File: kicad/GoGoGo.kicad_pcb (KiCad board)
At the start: 2 copper layers, 20.1 x 21.3 mm, 8 parts, among them P1 Vcc, P2 Input, P3 Output, U1 TB6593FNG

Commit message: Main layout done
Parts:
- moved C1 1.02 mm to (160.8, 86.9)
- moved C2 0.76 mm to (165.4, 86.6)
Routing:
- net /IN2: track 18.8 -> 14.0 mm
- net Net-(C1-Pad1): track 19.4 -> 17.3 mm
- net /IN1: track 13.8 -> 13.2 mm
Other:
- board text added: "GND"
- board text added: "IN1"
- board text added: "IN2"
- board text added: "Moto Driver Rev 2L.1"
- board text added: "O1"
- board text added: "O2"
- board text added: "PMW"
- board text added: "STBY"
- board text added: "Vcc"

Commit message: Gerbers created
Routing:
- net GND: track 0.00 -> 117.2 mm, vias 0 -> 84
- added copper zone on B.Cu, net GND

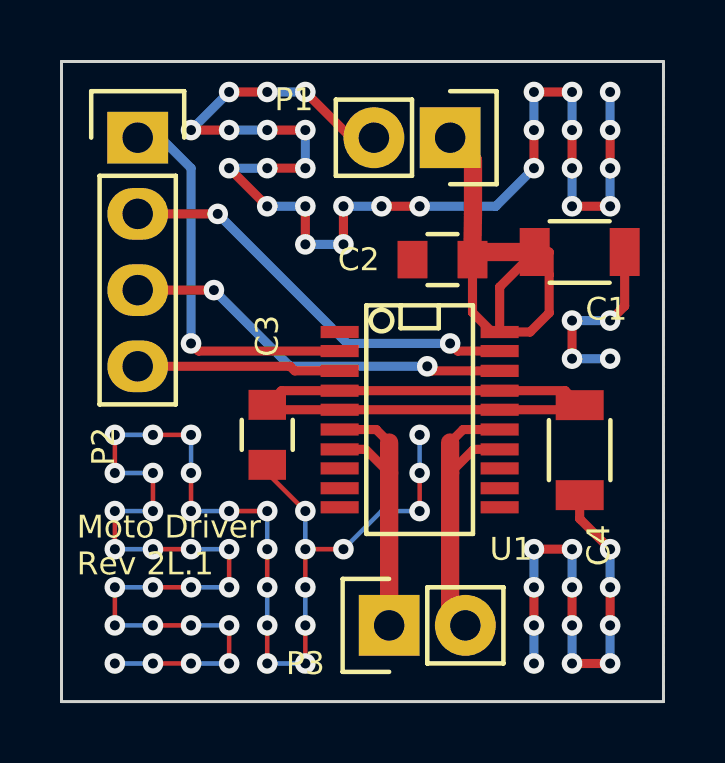
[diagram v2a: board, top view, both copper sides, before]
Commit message: Made corrections to the board based on the video on testing
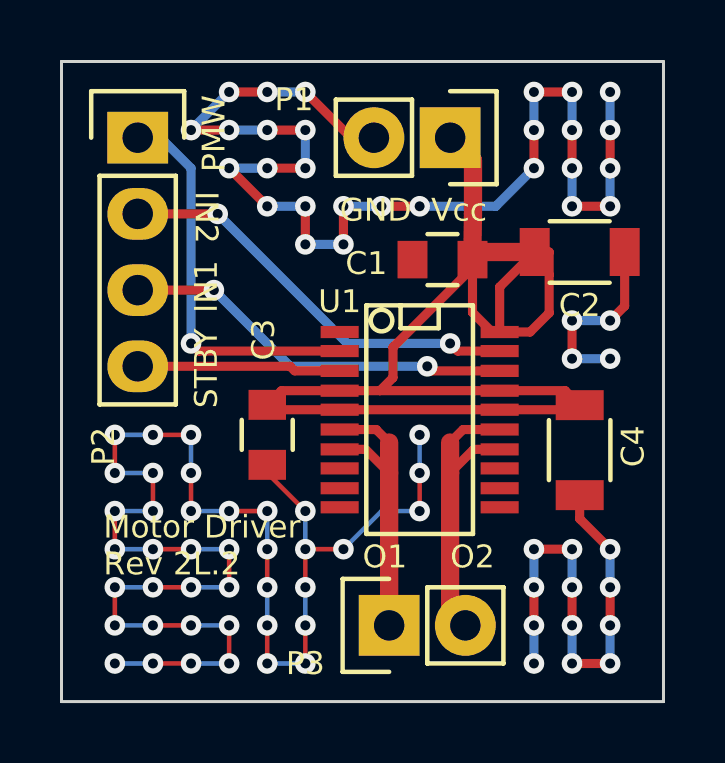
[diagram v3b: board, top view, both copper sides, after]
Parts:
- C1, C3: value 1u -> 0.1u
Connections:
- C1 pad 1: Net-(C1-Pad1) -> /VM
- C2 pad 1: Net-(C1-Pad1) -> /VM
- P1 pad 1: Net-(C1-Pad1) -> /VM
- U1 pad 20: Net-(C1-Pad1) -> /VM
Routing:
- net /VM: track 21.7 -> 44.6 mm
- net Net-(C1-Pad1): track 17.3 -> 0.00 mm
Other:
- board text added: "Motor Driver Rev 2L.2"
- board text removed: "Moto Driver Rev 2L.1"

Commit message: Added a small correction to a route
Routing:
- net /PMW: track 13.1 -> 11.3 mm
